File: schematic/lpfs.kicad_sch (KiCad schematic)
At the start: 51 parts

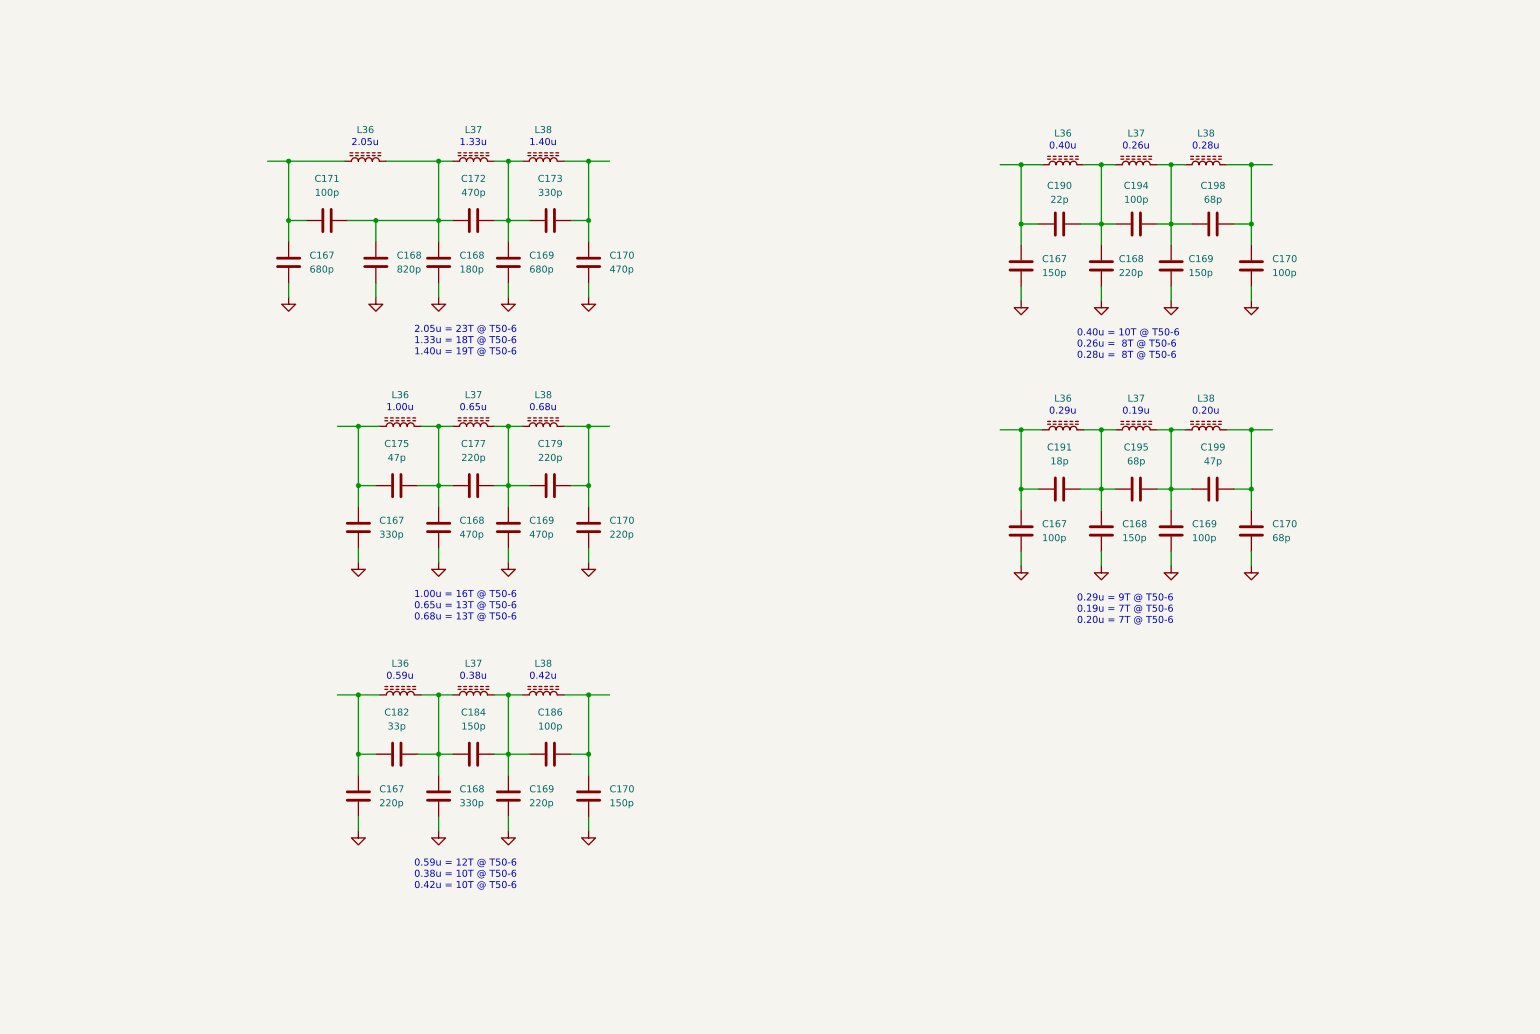
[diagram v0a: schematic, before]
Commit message: Schematic: add relays to /LPFs/ sheet
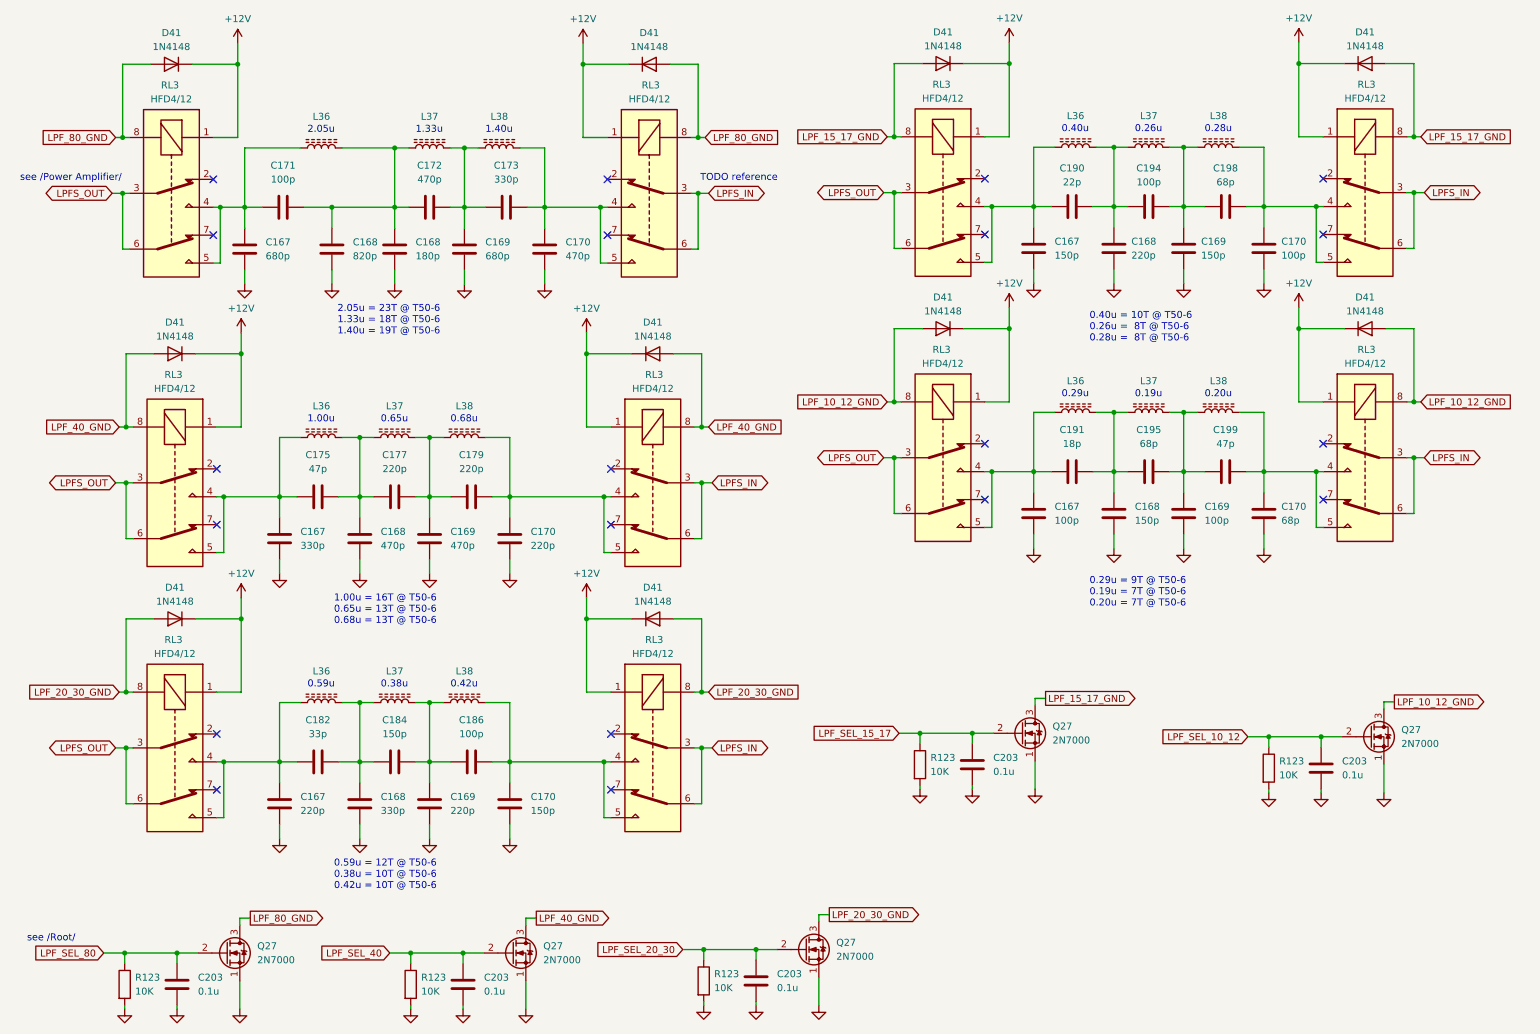
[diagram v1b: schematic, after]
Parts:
- added C203 (x5): 0.1u, symbol Device:C
- added D41 (x10): 1N4148, Diode_THT:D_DO-35_SOD27_P7.62mm_Horizontal, symbol Diode:1N4148
- added Q27 (x5): 2N7000, Package_TO_SOT_THT:TO-92_Inline, symbol Transistor_FET:2N7000
- added R123 (x5): 10K, symbol Device:R
- added RL3 (x10): HFD4/12, Relay_THT:Relay_DPDT_Omron_G2RL, symbol Relay:G2RL-2-ASI-DC5
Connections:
- net GND: now also C203.2, C203.2, C203.2, C203.2, C203.2, Q27.1 (S), Q27.1 (S), Q27.1 (S), Q27.1 (S), Q27.1 (S), R123.2, R123.2, R123.2, R123.2, R123.2
- net at C170.1, C198.2, L38.2: now also RL3.4, RL3.5
- net at C167.1, C182.1, L36.1: now also RL3.4, RL3.5
- net at C167.1, C191.1, L36.1: now also RL3.4, RL3.5
- net at C167.1, C190.1, L36.1: now also RL3.4, RL3.5
- net at C167.1, C171.1, L36.1: now also RL3.4, RL3.5
- net at C170.1, C186.2, L38.2: now also RL3.4, RL3.5
- net at C167.1, C175.1, L36.1: now also RL3.4, RL3.5
- net at C170.1, C173.2, L38.2: now also RL3.4, RL3.5
- net at C170.1, C199.2, L38.2: now also RL3.4, RL3.5
- net at C170.1, C179.2, L38.2: now also RL3.4, RL3.5
- new net +12V: D41.1 (K), D41.1 (K), D41.1 (K), D41.1 (K), D41.1 (K), D41.1 (K), D41.1 (K), D41.1 (K), D41.1 (K), D41.1 (K), RL3.1, RL3.1, RL3.1, RL3.1, RL3.1, RL3.1, RL3.1, RL3.1, RL3.1, RL3.1
- new net LPFS_IN: RL3.3, RL3.3, RL3.3, RL3.3, RL3.3, RL3.6, RL3.6, RL3.6, RL3.6, RL3.6
- new net LPFS_OUT: RL3.3, RL3.3, RL3.3, RL3.3, RL3.3, RL3.6, RL3.6, RL3.6, RL3.6, RL3.6
- new net LPF_10_12_GND: D41.2 (A), D41.2 (A), Q27.3 (D), RL3.8, RL3.8
- new net LPF_15_17_GND: D41.2 (A), D41.2 (A), Q27.3 (D), RL3.8, RL3.8
- new net LPF_20_30_GND: D41.2 (A), D41.2 (A), Q27.3 (D), RL3.8, RL3.8
- new net LPF_40_GND: D41.2 (A), D41.2 (A), Q27.3 (D), RL3.8, RL3.8
- new net LPF_80_GND: D41.2 (A), D41.2 (A), Q27.3 (D), RL3.8, RL3.8
- new net LPF_SEL_10_12: C203.1, Q27.2 (G), R123.1
- new net LPF_SEL_15_17: C203.1, Q27.2 (G), R123.1
- new net LPF_SEL_20_30: C203.1, Q27.2 (G), R123.1
- new net LPF_SEL_40: C203.1, Q27.2 (G), R123.1
- new net LPF_SEL_80: C203.1, Q27.2 (G), R123.1
- no-connect marks 0 -> 20
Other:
- note added: "TODO reference"
- note added: "see /Power Amplifier/"
- note added: "see /Root/"
- moved on the sheet: C167, C168, C169, C170, C171, C172, C173, C175, C177, C179, C182, C184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

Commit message: Schematic: minor changes
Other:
- moved on the sheet: C203, Q27, R123

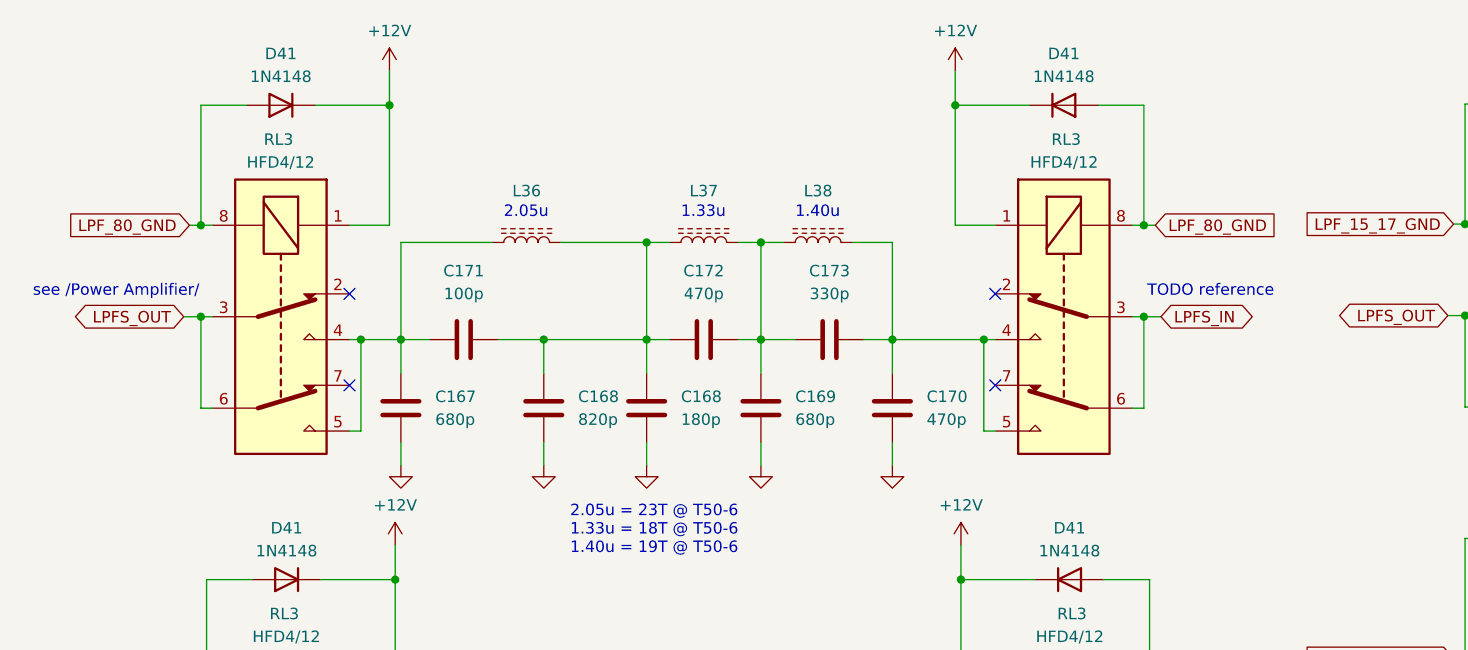
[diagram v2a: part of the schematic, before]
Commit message: Schematic: simplify 80M LPF
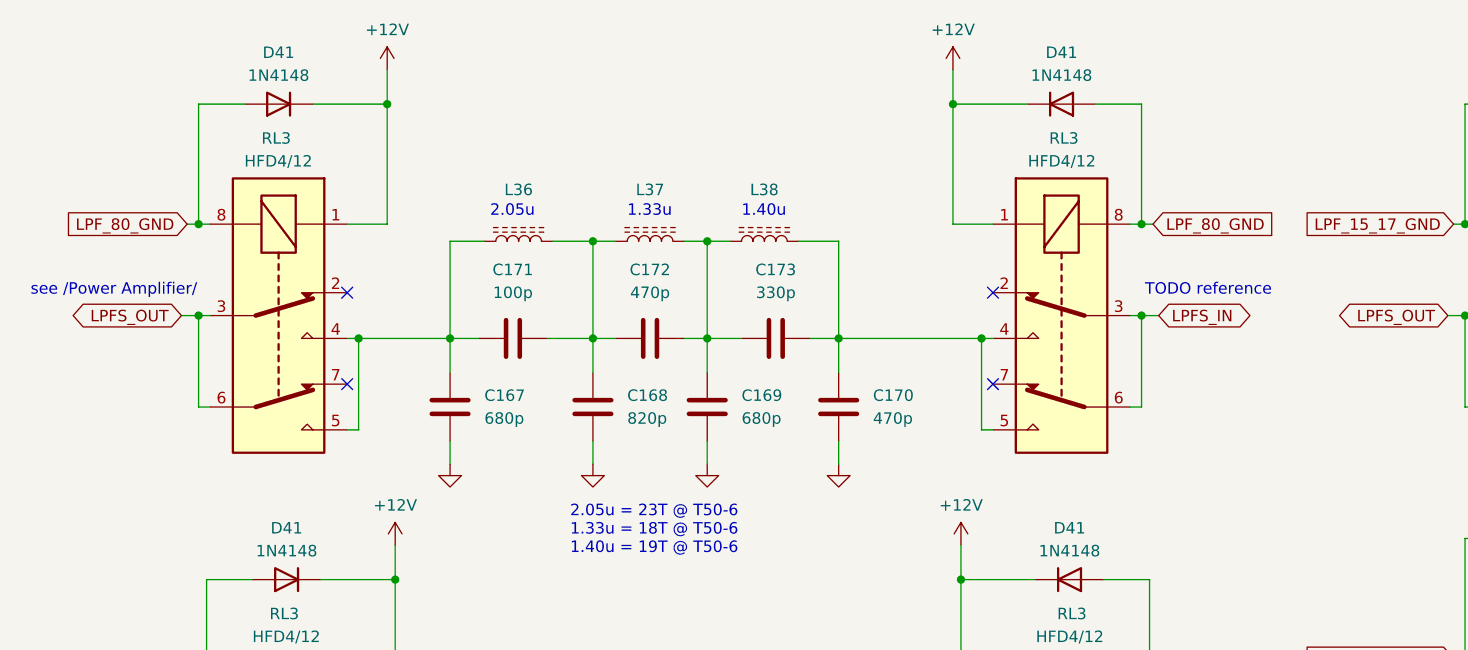
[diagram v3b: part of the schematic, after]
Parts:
- removed C168: 180p, symbol Device:C
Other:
- moved on the sheet: C167, C168, C169, C170, C171, C172, C173, L36, L37, L38

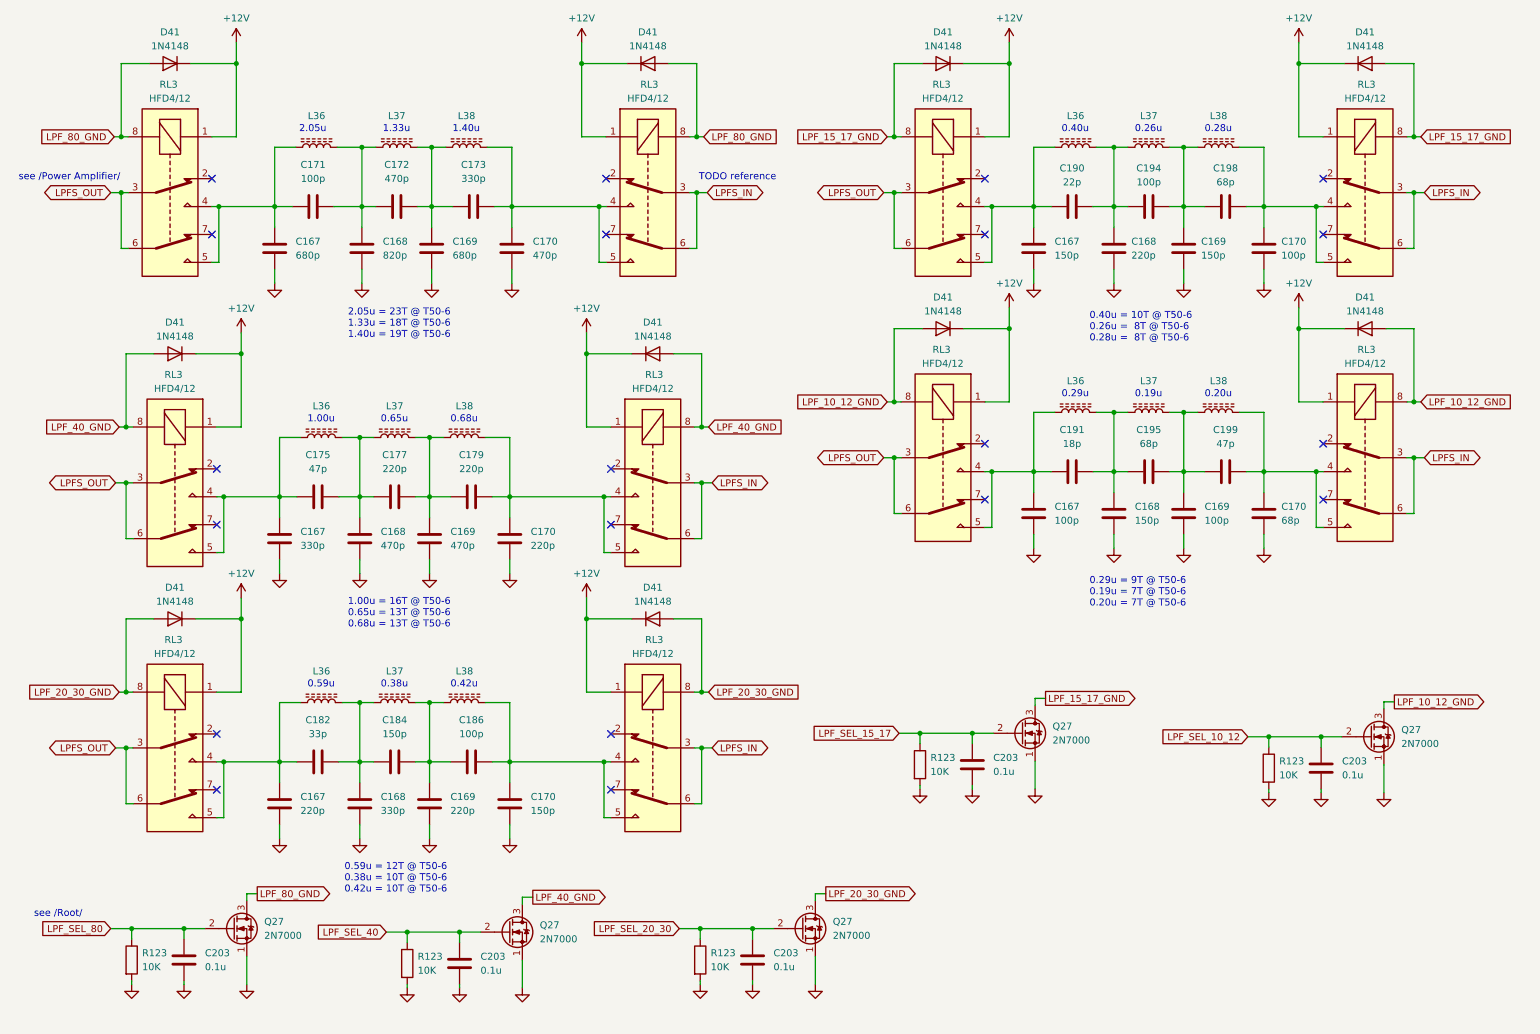
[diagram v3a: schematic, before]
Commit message: Schematic: correct number of turns for LPF inductors
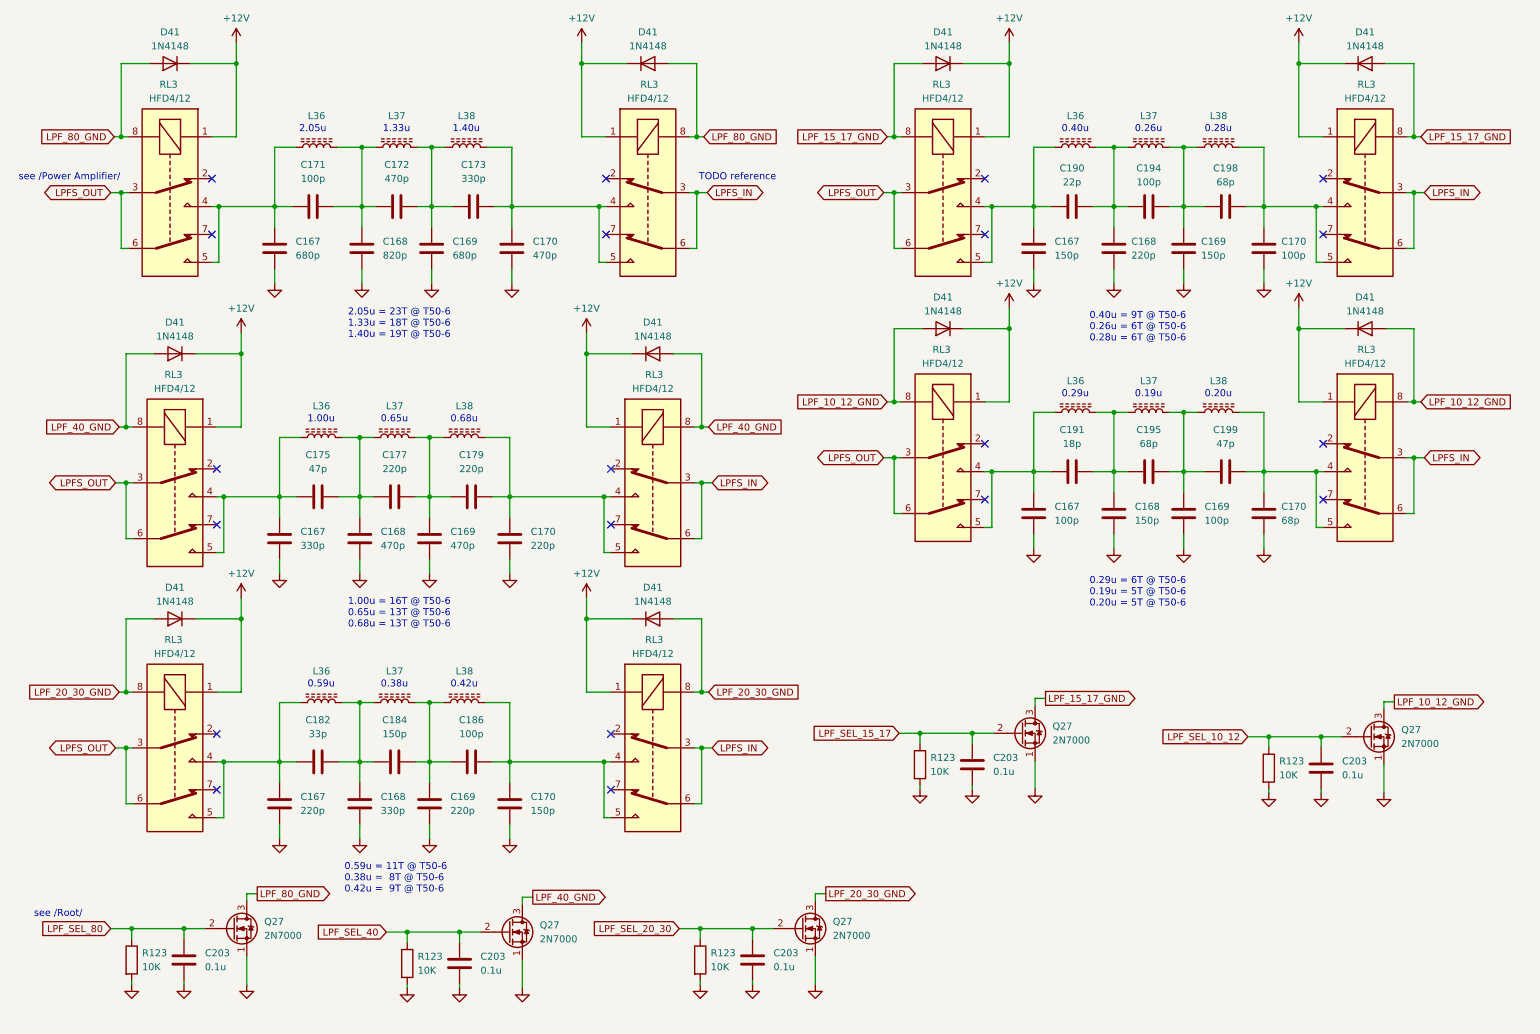
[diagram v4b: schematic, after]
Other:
- note added: "0.29u = 6T @ T50-6 0.19u = 5T @ T50-6 0.20u = 5T @ T50-6"
- note added: "0.40u = 9T @ T50-6 0.26u = 6T @ T50-6 0.28u = 6T @ T50-6"
- note added: "0.59u = 11T @ T50-6 0.38u = 8T @ T50-6 0.42u = 9T @ T50-6"
- note removed: "0.29u = 9T @ T50-6 0.19u = 7T @ T50-6 0.20u = 7T @ T50-6"
- note removed: "0.40u = 10T @ T50-6 0.26u = 8T @ T50-6 0.28u = 8T @ T50-6"
- note removed: "0.59u = 12T @ T50-6 0.38u = 10T @ T50-6 0.42u = 10T @ T50-6"
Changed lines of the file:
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@@
     (effects (font (size 1.27 1.27)) (justify left bottom))
   )
-  (text "0.40u = 10T @ T50-6\n0.26u =  8T @ T50-6\n0.28u =  8T @ T50-6"
+  (text "0.40u = 9T @ T50-6\n0.26u = 6T @ T50-6\n0.28u = 6T @ T50-6"
     (at 206.756 73.025 0)
     (effects (font (size 1.27 1.27)) (justify left bottom))
@@
     (effects (font (size 1.27 1.27)) (justify left bottom))
   )
-  (text "0.59u = 12T @ T50-6\n0.38u = 10T @ T50-6\n0.42u = 10T @ T50-6"
+  (text "0.59u = 11T @ T50-6\n0.38u =  8T @ T50-6\n0.42u =  9T @ T50-6"
     (at 71.12 173.355 0)
     (effects (font (size 1.27 1.27)) (justify left bottom))
@@
     (effects (font (size 1.27 1.27)) (justify left bottom))
   )
-  (text "0.29u = 9T @ T50-6\n0.19u = 7T @ T50-6\n0.20u = 7T @ T50-6"
+  (text "0.29u = 6T @ T50-6\n0.19u = 5T @ T50-6\n0.20u = 5T @ T50-6"
     (at 206.756 121.285 0)
     (effects (font (size 1.27 1.27)) (justify left bottom))

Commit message: Schematic: add SWR bridge
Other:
- note added: "see /SWR Bridge/"
- note removed: "TODO reference"
- moved on the sheet: D41, RL3

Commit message: Minor changes
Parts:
- renumbered C167 to C174, C168 to C176, C169 to C178, C170 to C180, C167 to C181, C168 to C183, C169 to C185, C170 to C187, C167 to C188, C167 to C189, C168 to C192, C168 to C193, C169 to C196, C169 to C197, C170 to C200, C170 to C201, C168 to C202, C203 to C204, C203 to C205, C203 to C206, C203 to C207, D41 to D42, D41 to D43, D41 to D44, D41 to D45, D41 to D46, D41 to D47, D41 to D48, D41 to D49, D41 to D50, L36 to L39, L37 to L40, L38 to L41, L36 to L42, L37 to L43, L38 to L44, L36 to L45, L36 to L46, L37 to L47, L37 to L48, L38 to L49, L38 to L50, Q27 to Q28, Q27 to Q29, Q27 to Q30, Q27 to Q31, R123 to R124, R123 to R125, R123 to R126, R123 to R127, RL3 to RL29, RL3 to RL30, RL3 to RL31, RL3 to RL32, RL3 to RL33, RL3 to RL34, RL3 to RL35, RL3 to RL36, RL3 to RL37, RL3 to RL38
